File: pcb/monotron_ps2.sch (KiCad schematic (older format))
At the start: 14 parts, among them J10 Mini-DIN-6, J11 Mini-DIN-6, J12 DB25_Female, J8 Conn_01x03_Male, J9 Conn_02x08_Odd_Even, SW1 SW_Push, U4 STM32F030C6Tx

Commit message: Changed to use Launchpad instead of bare chip. PS/2 handled by ATTINY24. LPT handled by MCP23017.
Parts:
- removed C23, C26, C27: 100n, symbol Device:C
- removed C24: 1u, symbol Device:C
- removed C25: 10n, symbol Device:C
- removed C28: 4.7u, symbol Device:C
- removed J8: Conn_01x03_Male, symbol Connector:Conn_01x03_Male
- removed J9: Conn_02x08_Odd_Even, symbol Connector_Generic:Conn_02x08_Odd_Even
- removed R4: 10K, symbol Device:R
- removed SW1: SW_Push, Button_Switch_THT:SW_PUSH_6mm, symbol Switch:SW_Push
- removed U4: STM32F030C6Tx, Package_QFP:LQFP-48_7x7mm_P0.5mm, symbol MCU_ST_STM32F0:STM32F030C6Tx
- added C13, C14: 100n, symbol Device:C
- added J9: AT_ISP, symbol Connector_Generic:Conn_02x03_Odd_Even
- added U4: ATtiny24A-PU, Package_DIP:DIP-14_W7.62mm, symbol MCU_Microchip_ATtiny:ATtiny24A-PU
- added U5: MCP23017_SP, Package_DIP:DIP-28_W7.62mm, symbol Interface_Expansion:MCP23017_SP
- renumbered J12 to J10, J10 to J11, J11 to J12
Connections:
- net labels added: INT_LPT, INT_PS2, IO_INT_LPT, IO_INT_PS2, IO_SCL, IO_SDA, MISO, MOSI_SDA, SCK_SCL, ~RESET
- net labels removed: +3.3V, GPIO0, GPIO1, GPIO10, GPIO11, GPIO12, GPIO2, GPIO3, GPIO4, GPIO5, GPIO6, GPIO7, GPIO8, GPIO9, UART_IO_TO_MCU, UART_MCU_TO_IO
- wire segments 156 -> 102
- no-connect marks 7 -> 8
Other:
- note removed: "EXT_INT_0\n"
- note removed: "EXT_INT_10\n"
- note removed: "EXT_INT_12\n"
- note removed: "EXT_INT_14"
- note removed: "EXT_INT_2"
- note removed: "EXT_INT_4"
- note removed: "EXT_INT_6\n"
- note removed: "EXT_INT_8"
- moved on the sheet: J10, J11, J12

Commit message: Adding footprints.
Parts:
- C11: renamed from C13; footprint (none) -> Capacitor_THT:C_Disc_D5.0mm_W2.5mm_P2.50mm
- C12: renamed from C14; footprint (none) -> Capacitor_THT:C_Disc_D5.0mm_W2.5mm_P2.50mm
- J10: footprint (none) -> Connector_Dsub:DSUB-25_Male_Horizontal_P2.77x2.84mm_EdgePinOffset7.70mm_Housed_MountingHolesOffset9.12mm; Digikey (none) -> 609-5920-ND
- J11, J12: Digikey (none) -> 5749180-1-ND
- J9: footprint (none) -> Connector_PinHeader_2.54mm:PinHeader_2x03_P2.54mm_Vertical
- renumbered U4 to U3, U5 to U4
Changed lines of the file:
@@
 F 1 "Mini-DIN-6" H 7500 2876 50  0000 C CNN
 F 2 "" H 7500 2600 50  0001 C CNN
-F 3 "http://service.powerdynamics.com/ec/Catalog17/Section%2011.pdf" H 7500 2600 50  0001 C CNN
+F 3 "https://www.te.com/commerce/DocumentDelivery/DDEController?Action=srchrtrv&DocNm=5749180&DocType=Customer+Drawing&DocLang=English" H 7500 2600 50  0001 C CNN
+F 4 "5749180-1-ND" H 7500 2600 50  0001 C CNN "Digikey"
 	1    7500 2600
 	1    0    0    -1
@@
 F 1 "Mini-DIN-6" H 7500 4026 50  0000 C CNN
 F 2 "" H 7500 3750 50  0001 C CNN
-F 3 "http://service.powerdynamics.com/ec/Catalog17/Section%2011.pdf" H 7500 3750 50  0001 C CNN
+F 3 "https://www.te.com/commerce/DocumentDelivery/DDEController?Action=srchrtrv&DocNm=5749180&DocType=Customer+Drawing&DocLang=English" H 7500 3750 50  0001 C CNN
+F 4 "5749180-1-ND" H 7500 3750 50  0001 C CNN "Digikey"
 	1    7500 3750
 	1    0    0    -1
@@
 F 0 "J10" H 5929 5496 50  0000 L CNN
 F 1 "DB25_Female" H 5929 5405 50  0000 L CNN
-F 2 "" H 5750 5450 50  0001 C CNN
-F 3 " ~" H 5750 5450 50  0001 C CNN
+F 2 "Connector_Dsub:DSUB-25_Male_Horizontal_P2.77x2.84mm_EdgePinOffset7.70mm_Housed_MountingHolesOffset9.12mm" H 5750 5450 50  0001 C CNN
+F 3 "http://portal.fciconnect.com/Comergent//fci/drawing/c-dd-0024.pdf" H 5750 5450 50  0001 C CNN
+F 4 "609-5920-ND" H 5750 5450 50  0001 C CNN "Digikey"
 	1    5750 5450
 	1    0    0    -1
@@
 Connection ~ 5300 5350
 $Comp
-L power:GND #PWR034
+L power:GND #PWR031
 U 1 1 5C870121
 P 5300 6850
-F 0 "#PWR034" H 5300 6600 50  0001 C CNN
+F 0 "#PWR031" H 5300 6600 50  0001 C CNN
 F 1 "GND" H 5305 6677 50  0000 C CNN
 F 2 "" H 5300 6850 50  0001 C CNN
@@
 	7800 3850 8150 3850
 $Comp
-L power:GND #PWR040
+L power:GND #PWR037
 U 1 1 5C89AC5C
 P 7900 3950
-F 0 "#PWR040" H 7900 3700 50  0001 C CNN
+F 0 "#PWR037" H 7900 3700 50  0001 C CNN
 F 1 "GND" H 7905 3777 50  0000 C CNN
 F 2 "" H 7900 3950 50  0001 C CNN
@@
 $EndComp
 $Comp
-L power:GND #PWR039
+L power:GND #PWR036
 U 1 1 5C89AC8A
 P 7900 2850
-F 0 "#PWR039" H 7900 2600 50  0001 C CNN
+F 0 "#PWR036" H 7900 2600 50  0001 C CNN
 F 1 "GND" H 7905 2677 50  0000 C CNN
 F 2 "" H 7900 2850 50  0001 C CNN
@@
 	7900 3750 7900 3950
 $Comp
-L power:+5V #PWR037
+L power:+5V #PWR034
 U 1 1 5C89CCFE
 P 6950 2450
-F 0 "#PWR037" H 6950 2300 50  0001 C CNN
+F 0 "#PWR034" H 6950 2300 50  0001 C CNN
 F 1 "+5V" H 6965 2623 50  0000 C CNN
 F 2 "" H 6950 2450 50  0001 C CNN
@@
 $EndComp
 $Comp
-L power:+5V #PWR038
+L power:+5V #PWR035
 U 1 1 5C89CD2C
 P 6950 3600
-F 0 "#PWR038" H 6950 3450 50  0001 C CNN
+F 0 "#PWR035" H 6950 3450 50  0001 C CNN
 F 1 "+5V" H 6965 3773 50  0000 C CNN
 F 2 "" H 6950 3600 50  0001 C CNN
@@
 ACK
 $Comp
-L MCU_Microchip_ATtiny:ATtiny24A-PU U4
+L MCU_Microchip_ATtiny:ATtiny24A-PU U3
 U 1 1 5C5DAFF6
 P 2250 2150
-F 0 "U4" H 1850 3000 50  0000 R CNN
+F 0 "U3" H 1850 3000 50  0000 R CNN
 F 1 "ATtiny24A-PU" H 2850 3000 50  0000 R CNN
 F 2 "Package_DIP:DIP-14_W7.62mm" H 2250 2150 50  0001 C CIN
@@
 $EndComp
 $Comp
-L Interface_Expansion:MCP23017_SP U5
+L Interface_Expansion:MCP23017_SP U4
 U 1 1 5C5DCA4D
 P 2250 5050
-F 0 "U5" H 2650 4050 50  0000 C CNN
+F 0 "U4" H 2650 4050 50  0000 C CNN
 F 1 "MCP23017_SP" H 1900 4050 50  0000 C CNN
 F 2 "Package_DIP:DIP-28_W7.62mm" H 2450 4050 50  0001 L CNN
@@
 D0
 $Comp
-L power:GND #PWR033
+L power:GND #PWR030
 U 1 1 5C5FA6DD
 P 3600 4550
-F 0 "#PWR033" H 3600 4300 50  0001 C CNN
+F 0 "#PWR030" H 3600 4300 50  0001 C CNN
 F 1 "GND" H 3605 4377 50  0000 C CNN
 F 2 "" H 3600 4550 50  0001 C CNN
@@
 STROBE
 $Comp
-L power:GND #PWR032
+L power:GND #PWR029
 U 1 1 5C61C7EA
 P 2250 6150
-F 0 "#PWR032" H 2250 5900 50  0001 C CNN
+F 0 "#PWR029" H 2250 5900 50  0001 C CNN
 F 1 "GND" H 2255 5977 50  0000 C CNN
 F 2 "" H 2250 6150 50  0001 C CNN
@@
 $EndComp
 $Comp
-L power:+5V #PWR031
+L power:+5V #PWR028
 U 1 1 5C61C92C
 P 2250 3950
-F 0 "#PWR031" H 2250 3800 50  0001 C CNN
+F 0 "#PWR028" H 2250 3800 50  0001 C CNN
 F 1 "+5V" H 2265 4123 50  0000 C CNN
 F 2 "" H 2250 3950 50  0001 C CNN
@@
 $EndComp
 $Comp
-L power:+5V #PWR029
+L power:+5V #PWR026
 U 1 1 5C61C941
 P 2250 1250
-F 0 "#PWR029" H 2250 1100 50  0001 C CNN
+F 0 "#PWR026" H 2250 1100 50  0001 C CNN
 F 1 "+5V" H 2265 1423 50  0000 C CNN
 F 2 "" H 2250 1250 50  0001 C CNN
@@
 $EndComp
 $Comp
-L power:GND #PWR030
+L power:GND #PWR027
 U 1 1 5C61CB48
 P 2250 3050
-F 0 "#PWR030" H 2250 2800 50  0001 C CNN
+F 0 "#PWR027" H 2250 2800 50  0001 C CNN
 F 1 "GND" H 2255 2877 50  0000 C CNN
 F 2 "" H 2250 3050 50  0001 C CNN
@@
 F 0 "J9" H 4950 2417 50  0000 C CNN
 F 1 "AT_ISP" H 4950 2326 50  0000 C CNN
-F 2 "" H 4900 2100 50  0001 C CNN
+F 2 "Connector_PinHeader_2.54mm:PinHeader_2x03_P2.54mm_Vertical" H 4900 2100 50  0001 C CNN
 F 3 "~" H 4900 2100 50  0001 C CNN
 	1    4900 2100
@@
 MISO
 $Comp
-L power:+5V #PWR035
+L power:+5V #PWR032
 U 1 1 5C656D6A
 P 5500 1850
-F 0 "#PWR035" H 5500 1700 50  0001 C CNN
+F 0 "#PWR032" H 5500 1700 50  0001 C CNN
 F 1 "+5V" H 5515 2023 50  0000 C CNN
 F 2 "" H 5500 1850 50  0001 C CNN
@@
 	5500 2000 5500 1850
 $Comp
-L power:GND #PWR036
+L power:GND #PWR033
 U 1 1 5C65A05C
 P 5500 2300
-F 0 "#PWR036" H 5500 2050 50  0001 C CNN
+F 0 "#PWR033" H 5500 2050 50  0001 C CNN
 F 1 "GND" H 5505 2127 50  0000 C CNN
 F 2 "" H 5500 2300 50  0001 C CNN
@@
 MOSI_SDA
 $Comp
-L power:+5V #PWR041
+L power:+5V #PWR038
 U 1 1 5C7704F7
 P 7900 4950
-F 0 "#PWR041" H 7900 4800 50  0001 C CNN
+F 0 "#PWR038" H 7900 4800 50  0001 C CNN
 F 1 "+5V" H 7915 5123 50  0000 C CNN
 F 2 "" H 7900 4950 50  0001 C CNN
@@
 $EndComp
 $Comp
-L power:GND #PWR042
+L power:GND #PWR039
 U 1 1 5C770515
 P 7900 5450
-F 0 "#PWR042" H 7900 5200 50  0001 C CNN
+F 0 "#PWR039" H 7900 5200 50  0001 C CNN
 F 1 "GND" H 7905 5277 50  0000 C CNN
 F 2 "" H 7900 5450 50  0001 C CNN
@@
 $EndComp
 $Comp
-L Device:C C13
+L Device:C C11
 U 1 1 5C77054A
 P 7700 5200
-F 0 "C13" H 7750 5300 50  0000 L CNN
+F 0 "C11" H 7750 5300 50  0000 L CNN
 F 1 "100n" H 7750 5100 50  0000 L CNN
-F 2 "" H 7738 5050 50  0001 C CNN
+F 2 "Capacitor_THT:C_Disc_D5.0mm_W2.5mm_P2.50mm" H 7738 5050 50  0001 C CNN
 F 3 "~" H 7700 5200 50  0001 C CNN
 	1    7700 5200
@@
 $EndComp
 $Comp
-L Device:C C14
+L Device:C C12
 U 1 1 5C77061D
 P 8100 5200
-F 0 "C14" H 8150 5300 50  0000 L CNN
+F 0 "C12" H 8150 5300 50  0000 L CNN
 F 1 "100n" H 8150 5100 50  0000 L CNN
-F 2 "" H 8138 5050 50  0001 C CNN
+F 2 "Capacitor_THT:C_Disc_D5.0mm_W2.5mm_P2.50mm" H 8138 5050 50  0001 C CNN
 F 3 "~" H 8100 5200 50  0001 C CNN
 	1    8100 5200

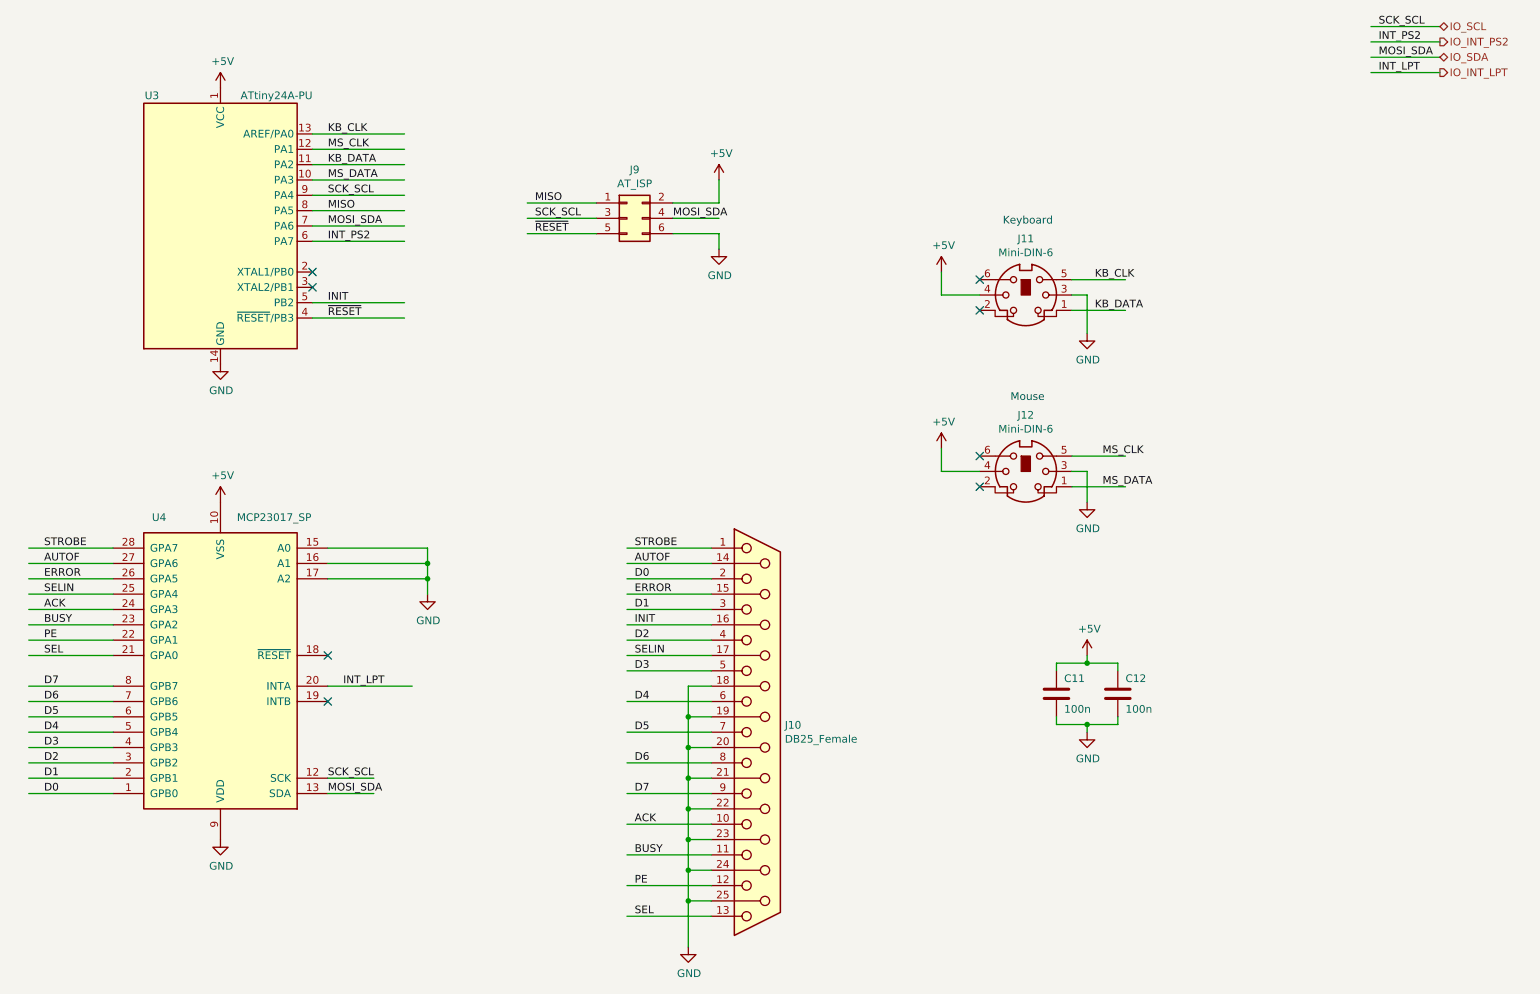
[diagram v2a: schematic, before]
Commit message: Added footprints. Change SD footprint for breakout board. Changed PS2/LPT interface to single AtMega48A. Moved MAX3232 to main sheet. Added I2C header. Started PCB layout.
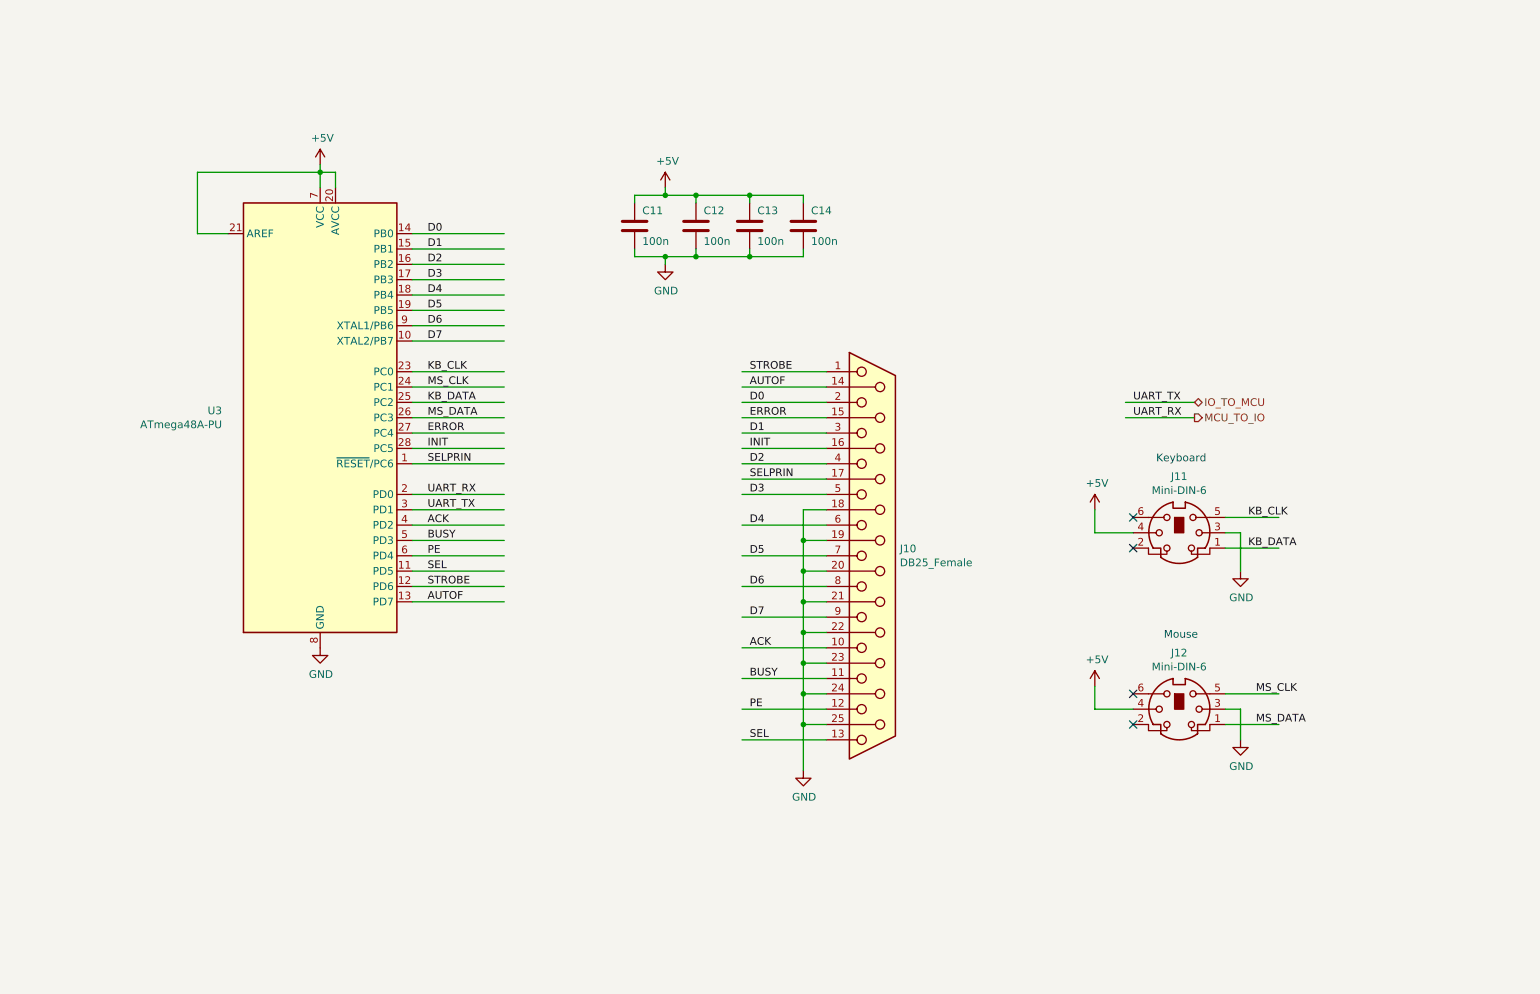
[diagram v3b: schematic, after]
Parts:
- removed J9: AT_ISP, Connector_PinHeader_2.54mm:PinHeader_2x03_P2.54mm_Vertical, symbol Connector_Generic:Conn_02x03_Odd_Even
- removed U3: ATtiny24A-PU, Package_DIP:DIP-14_W7.62mm, symbol MCU_Microchip_ATtiny:ATtiny24A-PU
- removed U4: MCP23017_SP, Package_DIP:DIP-28_W7.62mm, symbol Interface_Expansion:MCP23017_SP
- added C13, C14: 100n, Capacitor_THT:C_Disc_D5.0mm_W2.5mm_P2.50mm, symbol Device:C
- added U3: ATmega48A-PU, Package_DIP:DIP-28_W7.62mm, symbol MCU_Microchip_ATmega:ATmega48A-PU
- J11, J12: footprint (none) -> Connector_PinHeader_2.54mm:PinHeader_1x04_P2.54mm_Horizontal
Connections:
- net labels added: IO_TO_MCU, MCU_TO_IO, SELPRIN, UART_RX, UART_TX
- net labels removed: INT_LPT, INT_PS2, IO_INT_LPT, IO_INT_PS2, IO_SCL, IO_SDA, MISO, MOSI_SDA, SCK_SCL, SELIN, ~RESET
- wire segments 102 -> 95
- no-connect marks 8 -> 4
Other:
- moved on the sheet: C11, C12, J10, J11, J12

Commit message: Added MIDI interface.
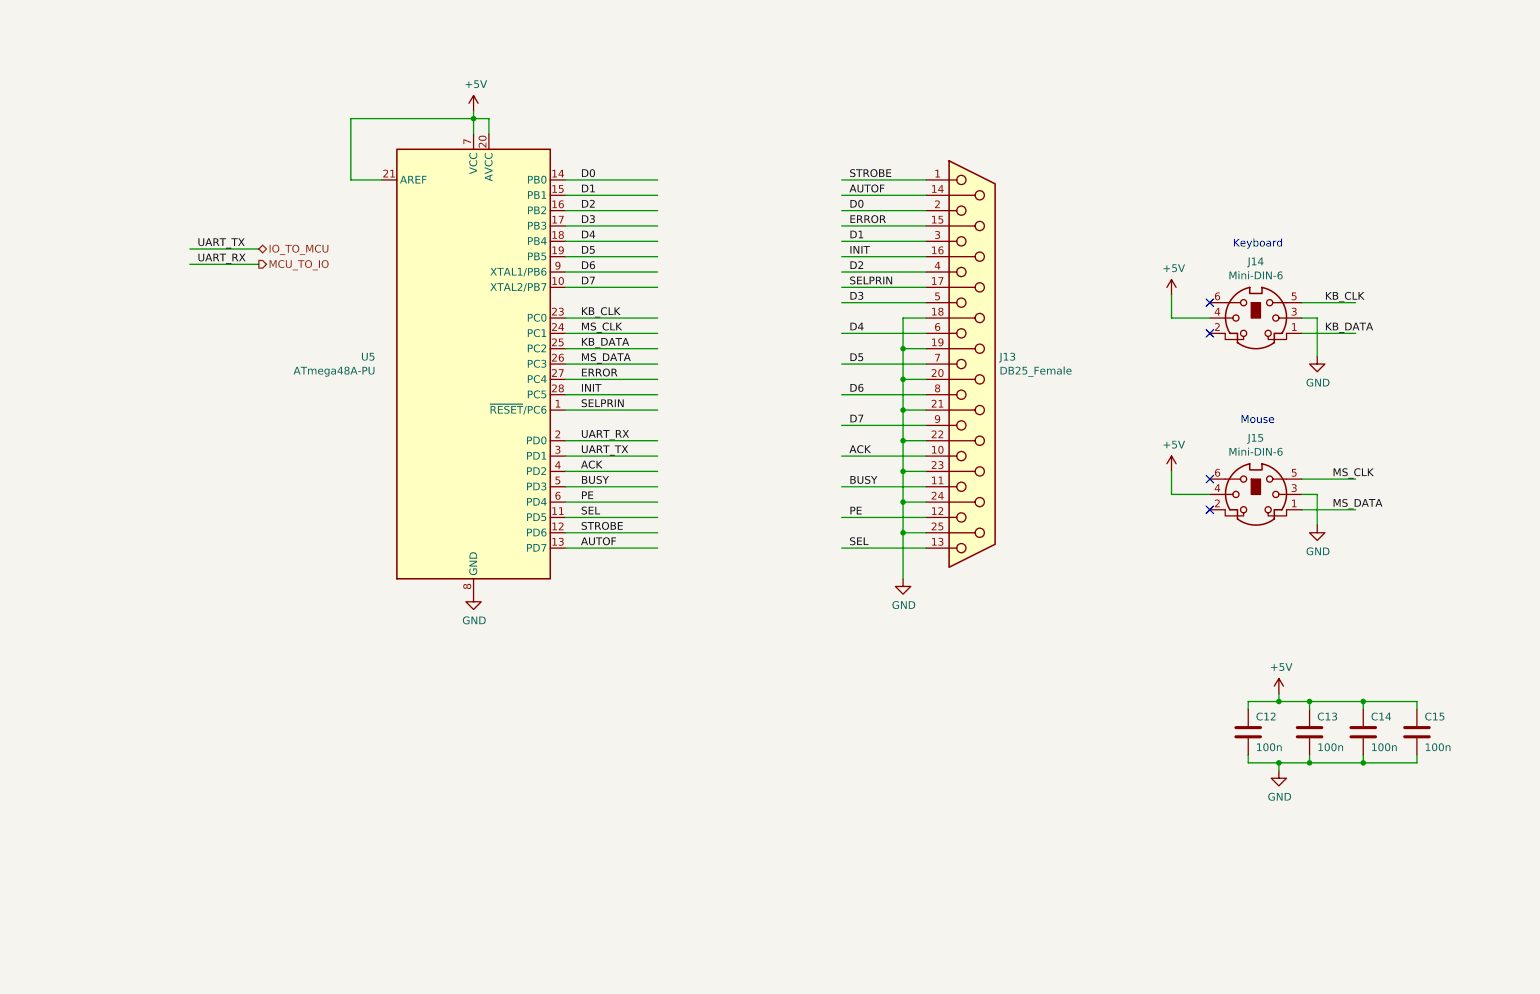
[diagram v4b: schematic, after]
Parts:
- renumbered C11 to C12, C12 to C13, C13 to C14, C14 to C15, J10 to J13, J11 to J14, J12 to J15, U3 to U5
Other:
- moved on the sheet: C12, C13, C14, C15, J13, J14, J15, U5

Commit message: Updated footprints.
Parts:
- J14, J15: footprint Connector_PinHeader_2.54mm:PinHeader_1x04_P2.54mm_Horizontal -> Launchpad:mini-DIN 6
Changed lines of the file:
@@
 F 0 "J14" H 9000 3117 50  0000 C CNN
 F 1 "Mini-DIN-6" H 9000 3026 50  0000 C CNN
-F 2 "Connector_PinHeader_2.54mm:PinHeader_1x04_P2.54mm_Horizontal" H 9000 2750 50  0001 C CNN
+F 2 "Launchpad:mini-DIN 6" H 9000 2750 50  0001 C CNN
 F 3 "https://www.te.com/commerce/DocumentDelivery/DDEController?Action=srchrtrv&DocNm=5749180&DocType=Customer+Drawing&DocLang=English" H 9000 2750 50  0001 C CNN
 F 4 "5749180-1-ND" H 9000 2750 50  0001 C CNN "Digikey"
@@
 F 0 "J15" H 9000 4267 50  0000 C CNN
 F 1 "Mini-DIN-6" H 9000 4176 50  0000 C CNN
-F 2 "Connector_PinHeader_2.54mm:PinHeader_1x04_P2.54mm_Horizontal" H 9000 3900 50  0001 C CNN
+F 2 "Launchpad:mini-DIN 6" H 9000 3900 50  0001 C CNN
 F 3 "https://www.te.com/commerce/DocumentDelivery/DDEController?Action=srchrtrv&DocNm=5749180&DocType=Customer+Drawing&DocLang=English" H 9000 3900 50  0001 C CNN
 F 4 "5749180-1-ND" H 9000 3900 50  0001 C CNN "Digikey"

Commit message: Primary component layout complete.
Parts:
- removed C15: 100n, Capacitor_THT:C_Disc_D5.0mm_W2.5mm_P2.50mm, symbol Device:C
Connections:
- wire segments 95 -> 91
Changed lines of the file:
@@
 Connection ~ 6700 2950
 $Comp
-L power:GND #PWR037
+L power:GND #PWR035
 U 1 1 5C870121
 P 6700 4450
-F 0 "#PWR037" H 6700 4200 50  0001 C CNN
+F 0 "#PWR035" H 6700 4200 50  0001 C CNN
 F 1 "GND" H 6705 4277 50  0000 C CNN
 F 2 "" H 6700 4450 50  0001 C CNN
@@
 	9400 3900 9400 4100
 $Comp
-L power:+5V #PWR038
+L power:+5V #PWR036
 U 1 1 5C89CCFE
 P 8450 2600
-F 0 "#PWR038" H 8450 2450 50  0001 C CNN
+F 0 "#PWR036" H 8450 2450 50  0001 C CNN
 F 1 "+5V" H 8465 2773 50  0000 C CNN
 F 2 "" H 8450 2600 50  0001 C CNN
@@
 $EndComp
 $Comp
-L power:+5V #PWR039
+L power:+5V #PWR037
 U 1 1 5C89CD2C
 P 8450 3750
-F 0 "#PWR039" H 8450 3600 50  0001 C CNN
+F 0 "#PWR037" H 8450 3600 50  0001 C CNN
 F 1 "+5V" H 8465 3923 50  0000 C CNN
 F 2 "" H 8450 3750 50  0001 C CNN
@@
 UART_TX
 $Comp
-L power:+5V #PWR035
+L power:+5V #PWR038
 U 1 1 5C7704F7
 P 9150 5200
-F 0 "#PWR035" H 9150 5050 50  0001 C CNN
+F 0 "#PWR038" H 9150 5050 50  0001 C CNN
 F 1 "+5V" H 9165 5373 50  0000 C CNN
 F 2 "" H 9150 5200 50  0001 C CNN
@@
 $EndComp
 $Comp
-L power:GND #PWR036
+L power:GND #PWR039
 U 1 1 5C770515
 P 9150 5700
-F 0 "#PWR036" H 9150 5450 50  0001 C CNN
+F 0 "#PWR039" H 9150 5450 50  0001 C CNN
 F 1 "GND" H 9155 5527 50  0000 C CNN
 F 2 "" H 9150 5700 50  0001 C CNN
@@
 	1    0    0    -1
 $EndComp
-$Comp
-L Device:C C15
-U 1 1 5C35D061
-P 10050 5450
-F 0 "C15" H 10100 5550 50  0000 L CNN
-F 1 "100n" H 10100 5350 50  0000 L CNN
-F 2 "Capacitor_THT:C_Disc_D5.0mm_W2.5mm_P2.50mm" H 10088 5300 50  0001 C CNN
-F 3 "~" H 10050 5450 50  0001 C CNN
-	1    10050 5450
-	1    0    0    -1
-$EndComp
 Wire Wire Line
 	9350 5650 9700 5650
-Wire Wire Line
-	10050 5650 10050 5600
 Connection ~ 9350 5650
 Wire Wire Line
 	9700 5600 9700 5650
-Connection ~ 9700 5650
-Wire Wire Line
-	9700 5650 10050 5650
 Wire Wire Line
 	9350 5250 9700 5250
@@
 	9700 5250 9700 5300
 Connection ~ 9350 5250
-Wire Wire Line
-	9700 5250 10050 5250
-Wire Wire Line
-	10050 5250 10050 5300
-Connection ~ 9700 5250
 $EndSCHEMATC
